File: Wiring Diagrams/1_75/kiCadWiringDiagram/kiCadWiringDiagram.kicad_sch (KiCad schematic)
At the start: 28 parts, among them J1 ESP32, J12 Speaker Connector, J2 Encoder Connector, J3 LED Connector, J4 Motor Connector, J5 12v Input 1, J6 12v Input 2, U1 LM2596S-5, U2 MC34063AD, U3 MMC5603NJ, U4 TMC6300-LA, U5 MCP23017_ML

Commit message: Schematic now done I think
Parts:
- added C7, C8: C_Small, symbol Device:C_Small
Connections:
- net at C2.2, C3.2, C4.2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: now also U5.11 (A0), U5.12 (A1), U5.13 (A2), U5.6 (VSS), C7.2
- net at J1.3 (Pin_3), J2.1 (Pin_1), U3.B1 (VDD)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: now also U5.14 (~{RESET}), U5.5 (VDD)
- net at J1.7 (Pin_7), U3.B2 (SDA): now also U5.9 (SDA)
- net at J1.8 (Pin_8), U3.A2 (SCL): now also U5.8 (SCK)
- net at U5.17 (GPA0): now also U4.7 (WL)
- net at U5.18 (GPA1): now also U4.5 (WH)
- net at U5.19 (GPA2): now also U4.10 (VL)
- net at U5.20 (GPA3): now also U4.4 (VH)
- net at U5.21 (GPA4): now also U4.6 (UL)
- net at U5.22 (GPA5): now also U4.3 (UH)
- net at U4.13 (1.8VOUT): now also C7.1
- net at C5.1, D4.1 (K), R2.2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: now also C8.2
- net at U4.2 (VCP): now also C8.1
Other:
- moved on the sheet: C1, C2, C3, C4, C5, C6, D1, D2, D3, D4, F1, F2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

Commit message: pull up resisters added to i2c bus
now finished schematic I think
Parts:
- added R3, R4: R_Small, symbol Device:R_Small
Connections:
- net at U3.B2 (SDA), U5.9 (SDA): now also R4.2; no longer J1.7 (Pin_7)
- net at U3.A2 (SCL), U5.8 (SCK): now also R3.2; no longer J1.8 (Pin_8)
- new net: J1.7 (Pin_7), R4.1
- new net: J1.8 (Pin_8), R3.1
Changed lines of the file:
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@@
 	(wire
 		(pts
+			(xy 217.17 88.9) (xy 217.17 96.52)
+		)
+		(stroke
+			(width 0)
+			(type default)
+		)
+	)
+	(wire
+		(pts
 			(xy 110.49 151.13) (xy 110.49 154.94)
 		)
@@
 	(wire
 		(pts
-			(xy 214.63 73.66) (xy 214.63 99.06)
+			(xy 214.63 73.66) (xy 214.63 83.82)
 		)
 		(stroke
@@
 	(wire
 		(pts
-			(xy 217.17 73.66) (xy 217.17 96.52)
+			(xy 217.17 73.66) (xy 217.17 83.82)
 		)
 		(stroke
@@
 	(wire
 		(pts
+			(xy 214.63 88.9) (xy 214.63 99.06)
+		)
+		(stroke
+			(width 0)
+			(type default)
+		)
+	)
+	(wire
+		(pts
 			(xy 233.68 109.22) (xy 265.43 109.22)
 		)
@@
 	)
 	(symbol
+		(lib_id "Device:R_Small")
+		(at 217.17 86.36 0)
+		(unit 1)
+		(exclude_from_sim no)
+		(in_bom yes)
+		(on_board yes)
+		(dnp no)
+		(property "Reference" "R3"
+			(at 218.44 86.106 0)
+			(effects
+				(font
+					(size 1.016 1.016)
+				)
+				(justify left)
+			)
+		)
+		(property "Value" "R_Small"
+			(at 218.44 89.408 0)
+			(effects
+				(font
+					(size 1.27 1.27)
+				)
+				(justify left)
+			)
+		)
+		(property "Footprint" ""
+			(at 217.17 86.36 0)
+			(effects
+				(font
+					(size 1.27 1.27)
+				)
+				(hide yes)
+			)
+		)
+		(property "Datasheet" "~"
+			(at 217.17 86.36 0)
+			(effects
+				(font
+					(size 1.27 1.27)
+				)
+				(hide yes)
+			)
+		)
+		(property "Description" "Resistor, small symbol"
+			(at 217.17 86.36 0)
+			(effects
+				(font
+					(size 1.27 1.27)
+				)
+				(hide yes)
+			)
+		)
+		(pin "1"
+		)
+		(pin "2"
+		)
+		(instances
+			(project ""
+				(path "/98b16ca0-9240-4131-a459-a4d203a19b3c"
+					(reference "R3")
+					(unit 1)
+				)
+			)
+		)
+	)
+	(symbol
 		(lib_id "Device:C_Small")
 		(at 80.01 83.82 90)
@@
 					(unit 1)
 				)
+			)
+		)
+	)
+	(symbol
+		(lib_id "Device:R_Small")
+		(at 214.63 86.36 0)
+		(unit 1)
+		(exclude_from_sim no)
+		(in_bom yes)
+		(on_board yes)
+		(dnp no)
+		(property "Reference" "R4"
+			(at 211.328 86.106 0)
+			(effects
+				(font
+					(size 1.016 1.016)
+				)
+				(justify left)
+			)
+		)
+		(property "Value" "R_Small"
+			(at 205.994 89.408 0)
+			(effects
+				(font
+					(size 1.27 1.27)
+				)
+				(justify left)
+			)
+		)
+		(property "Footprint" ""
+			(at 214.63 86.36 0)
+			(effects
+				(font
+					(size 1.27 1.27)
+				)
+				(hide yes)
+			)
+		)
+		(property "Datasheet" "~"
+			(at 214.63 86.36 0)
+			(effects
+				(font
+					(size 1.27 1.27)
+				)
+				(hide yes)
+			)
+		)
+		(property "Description" "Resistor, small symbol"
+			(at 214.63 86.36 0)
+			(effects
+				(font
+					(size 1.27 1.27)
+				)
+				(hide yes)
+			)
+		)
+		(pin "1"
+		)
+		(pin "2"
+		)
+		(instances
+			(project "kiCadWiringDiagram"
+				(path "/98b16ca0-9240-4131-a459-a4d203a19b3c"
+					(reference "R4")
+					(unit 1)
+				)

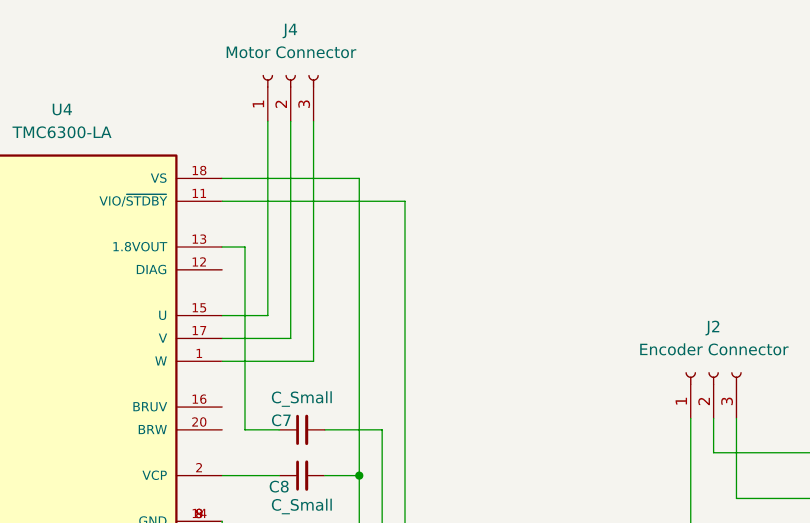
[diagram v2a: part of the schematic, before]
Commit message: Started Footprint assignments
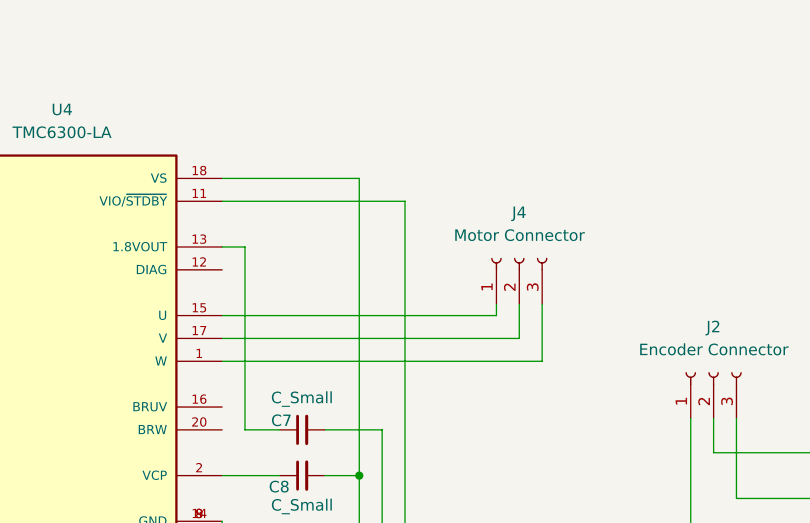
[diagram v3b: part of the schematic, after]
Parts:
- J1: footprint (none) -> Connector_JST:JST_XH_S10B-XH-A-1_1x10_P2.50mm_Horizontal
- J12: footprint (none) -> Connector_JST:JST_GH_BM02B-GHS-TBT_1x02-1MP_P1.25mm_Vertical
- J2, J3, J4: footprint (none) -> Connector_JST:JST_XH_S3B-XH-A-1_1x03_P2.50mm_Horizontal
- J5, J6: footprint (none) -> Connector_JST:JST_XH_S2B-XH-A-1_1x02_P2.50mm_Horizontal
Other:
- moved on the sheet: J4
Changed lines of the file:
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@@
 	(wire
 		(pts
-			(xy 76.2 66.04) (xy 71.12 66.04)
-		)
-		(stroke
-			(width 0)
-			(type default)
-		)
-	)
-	(wire
-		(pts
 			(xy 27.94 121.92) (xy 36.83 121.92)
 		)
@@
 	(wire
 		(pts
+			(xy 101.6 64.77) (xy 101.6 66.04)
+		)
+		(stroke
+			(width 0)
+			(type default)
+		)
+	)
+	(wire
+		(pts
 			(xy 73.66 78.74) (xy 77.47 78.74)
 		)
@@
 	(wire
 		(pts
+			(xy 101.6 66.04) (xy 71.12 66.04)
+		)
+		(stroke
+			(width 0)
+			(type default)
+		)
+	)
+	(wire
+		(pts
 			(xy 144.78 77.47) (xy 144.78 81.28)
 		)
@@
 	(wire
 		(pts
-			(xy 78.74 68.58) (xy 71.12 68.58)
+			(xy 104.14 68.58) (xy 71.12 68.58)
 		)
 		(stroke
@@
 	(wire
 		(pts
-			(xy 81.28 71.12) (xy 71.12 71.12)
+			(xy 106.68 71.12) (xy 71.12 71.12)
 		)
 		(stroke
@@
 	(wire
 		(pts
-			(xy 76.2 44.45) (xy 76.2 66.04)
-		)
-		(stroke
-			(width 0)
-			(type default)
-		)
-	)
-	(wire
-		(pts
 			(xy 72.39 129.54) (xy 74.93 129.54)
 		)
@@
 	(wire
 		(pts
-			(xy 81.28 44.45) (xy 81.28 71.12)
+			(xy 106.68 64.77) (xy 106.68 71.12)
 		)
 		(stroke
@@
 	(wire
 		(pts
-			(xy 78.74 44.45) (xy 78.74 68.58)
+			(xy 104.14 64.77) (xy 104.14 68.58)
 		)
 		(stroke
@@
 	(symbol
 		(lib_id "Connector:Conn_01x03_Socket")
-		(at 78.74 39.37 90)
+		(at 104.14 59.69 90)
 		(unit 1)
 		(exclude_from_sim no)
@@
 		(fields_autoplaced yes)
 		(property "Reference" "J4"
-			(at 78.74 34.29 90)
+			(at 104.14 54.61 90)
 			(effects
 				(font
@@
 		)
 		(property "Value" "Motor Connector"
-			(at 78.74 36.83 90)
+			(at 104.14 57.15 90)
 			(effects
 				(font
@@
 			)
 		)
-		(property "Footprint" ""
-			(at 78.74 39.37 0)
+		(property "Footprint" "Connector_JST:JST_XH_S3B-XH-A-1_1x03_P2.50mm_Horizontal"
+			(at 104.14 59.69 0)
 			(effects
 				(font
@@
 		)
 		(property "Datasheet" "~"
-			(at 78.74 39.37 0)
+			(at 104.14 59.69 0)
 			(effects
 				(font
@@
 		)
 		(property "Description" "Generic connector, single row, 01x03, script generated"
-			(at 78.74 39.37 0)
+			(at 104.14 59.69 0)
 			(effects
 				(font
@@
 			)
 		)
-		(property "Footprint" ""
+		(property "Footprint" "Connector_JST:JST_XH_S10B-XH-A-1_1x10_P2.50mm_Horizontal"
 			(at 209.55 68.58 0)
 			(effects
@@
 			)
 		)
-		(property "Footprint" ""
+		(property "Footprint" "Connector_JST:JST_XH_S2B-XH-A-1_1x02_P2.50mm_Horizontal"
 			(at 168.91 149.86 0)
 			(effects
@@
 			)
 		)
-		(property "Footprint" ""
+		(property "Footprint" "Connector_JST:JST_XH_S3B-XH-A-1_1x03_P2.50mm_Horizontal"
 			(at 125.73 72.39 0)
 			(effects
@@
 			)
 		)
-		(property "Footprint" ""
+		(property "Footprint" "Connector_JST:JST_GH_BM02B-GHS-TBT_1x02-1MP_P1.25mm_Vertical"
 			(at 265.43 78.74 0)
 			(effects
@@
 			)
 		)
-		(property "Footprint" ""
+		(property "Footprint" "Connector_JST:JST_XH_S2B-XH-A-1_1x02_P2.50mm_Horizontal"
 			(at 189.23 149.86 0)
 			(effects
@@
 			)
 		)
-		(property "Footprint" ""
+		(property "Footprint" "Connector_JST:JST_XH_S3B-XH-A-1_1x03_P2.50mm_Horizontal"
 			(at 144.78 72.39 0)
 			(effects

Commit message: Completed footprints
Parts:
- C1, C6, C7, C8: footprint (none) -> Capacitor_SMD:C_0805_2012Metric
- C2, C3, C4, C5: footprint (none) -> Capacitor_SMD:CP_Elec_6.3x5.4
- D1, D2, D3, D4: footprint (none) -> Diode_SMD:D_SMA
- F1, F2: footprint (none) -> Fuse:Fuse_1206_3216Metric
- L1, L2: footprint (none) -> Inductor_SMD:L_7.3x7.3_H4.5
- R1, R2, R3, R4: footprint (none) -> Resistor_SMD:R_0805_2012Metric
- renumbered J12 to J7
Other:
- moved on the sheet: C1, C2, C3, D1, D2, D3, F1, F2, J1, J5, J6, J7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

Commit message: update
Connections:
- net GND: now reaches C2.2, C3.2, C4.2, C5.2, C6.2, C7.2, D3.2 (A), J1.2 (Pin_2), J2.2 (Pin_2), J3.2 (Pin_2), J5.1 (Pin_1), J6.1 (Pin_1), R1.2, U1.3 (GND), U1.5 (~{ON}/OFF), U2.2 (SwE), U2.4 (GND), U3.A1 (VSA), U4.14 (GND), U4.21 (EXP), U4.8 (GND), U4.9 (GND), U5.11 (A0), U5.12 (A1), U5.13 (A2), U5.6 (VSS)
- net GND: no longer J1.1 (Pin_1), J3.1 (Pin_1)
- net +3V3: now reaches J1.3 (Pin_3), J2.1 (Pin_1), U3.B1 (VDD), U4.11 (VIO/~{STDBY}), U5.14 (~{RESET}), U5.5 (VDD)
- net +5V: now reaches C3.1, C4.1, L1.1, L2.1, U1.4 (FB), U2.6 (Vin), U2.7 (Ipk), U2.8 (DC)
- net +5V: now also J1.1 (Pin_1), J3.1 (Pin_1)
- net +12V: now reaches F1.2, J6.2 (Pin_2)
- net +12V: now also C1.1, C1.2, C2.1, D1.1 (K), D1.2 (A), D2.1 (K), D2.2 (A), F1.1, F2.1, F2.2, J5.2 (Pin_2), U1.1 (VIN)
- net +10V: now reaches C5.1, C8.2, D4.1 (K), R2.2, U4.18 (VS)
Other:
- note added: "12V to 5V Conversion"
- note added: "5V to 10V Conversion"
- note added: "Dual Power Inputs"
- note added: "GPIO Extension"
- note added: "Magnetometer"
- note added: "Motor Driver IC"
- note removed: "5V Negative"
- note removed: "5V Positive"
- moved on the sheet: J5, J6
